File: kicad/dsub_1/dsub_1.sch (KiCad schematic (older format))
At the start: 3 parts, among them J1 DB15_Female, J2 DB15_Female, J3 DB25_Female

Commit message: geändert:       Doku/Anmerungen_fuer_Doku.odt 	geändert:       Doku/Tagebuch_Ziele.odt 	geändert:       abschlussprojekt/abschlussprojekt.ino -> Helligkeitssensor + LEDs implementiert 	geändert:       kicad/dsub_1/dsub_1.bak 	geändert:       kicad/dsub_1/dsub_1.pdf 	geändert:       kicad/dsub_1/dsub_1.sch
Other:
- note added: "Leistung:\nLüfter -> 12V/0,11A\nHeizung -> 12V/4,5A (55W)\nLEDs -> rot 12V/80mA; blau 12V/80mA\nPumpe -> 3-5V/100-200mA\n"
- note removed: "Leistung:\nLüfter -> 12V/0,11A\nHeizung -> 12V, 55W\nLEDs -> sehr wenig\nPumpe -> 3-5V/100-200mA\n"
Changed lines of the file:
@@
 Stecker:\nTorsten -> Männchen, Male\nFabian -> Weibchen, Female
 Text Notes 700  5250 0    79   ~ 0
-Leistung:\nLüfter  -> 12V/0,11A\nHeizung -> 12V, 55W\nLEDs   -> sehr wenig\nPumpe -> 3-5V/100-200mA\n
+Leistung:\nLüfter  -> 12V/0,11A\nHeizung -> 12V/4,5A  (55W)\nLEDs   -> rot 12V/80mA; blau 12V/80mA\nPumpe -> 3-5V/100-200mA\n
 $Comp
 L Connector:DB15_Female J2

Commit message: geändert:       abschlussprojekt/abschlussprojekt.ino 	gelöscht:       abschlussprojekt/update_limits.h 	neue Datei:     abschlussprojekt/update_messwerte.c 	neue Datei:     abschlussprojekt/update_messwerte.h 	geändert:       kicad/dsub_1/dsub_1-cache.lib 	geändert:       kicad/dsub_1/dsub_1.bak 	geändert:       kicad/dsub_1/dsub_1.pdf 	geändert:       kicad/dsub_1/dsub_1.sch
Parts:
- removed J1, J2: DB15_Female, symbol Connector:DB15_Female
- added J?: Conn_01x02, symbol Connector_Generic:Conn_01x02
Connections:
- net Heizung_minus: now also J?.1 (Pin_1); no longer J3.18 (P18)
- net Heizung_plus: now also J?.2 (Pin_2); no longer J3.19 (P19)
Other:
- note added: "Leistung:\nHeizung -> 12V/4,5A (55W)\nPumpe -> 3-5V/200-360mA\nLüfter -> 12V/0,11A\nLEDs -> rot 12V/80mA; blau 12V/80mA"
- note added: "extra Stecker, \nweil zuviel Strom für SubD"
- note removed: "Leistung:\nLüfter -> 12V/0,11A\nHeizung -> 12V/4,5A (55W)\nLEDs -> rot 12V/80mA; blau 12V/80mA\nPumpe -> 3-5V/100-200mA\n"
- note removed: "Signalkabel und stromführende Kabel\nin einem Stecker -> Problem Störungen, EMV ?"
- note removed: "Stecker Signale"
- note removed: "Stecker Stromführung"
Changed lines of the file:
@@
 Wire Wire Line
 	7950 3600 9550 3600
-$Comp
-L Connector:DB15_Female J1
-U 1 1 5D76075D
-P 5100 2500
-F 0 "J1" H 5007 1508 50  0000 C CNN
-F 1 "DB15_Female" H 5007 1599 50  0000 C CNN
-F 2 "" H 5100 2500 50  0001 C CNN
-F 3 " ~" H 5100 2500 50  0001 C CNN
-	1    5100 2500
-	1    0    0    1
-$EndComp
-Text GLabel 4500 3200 0    50   Input ~ 0
-Erdfeuchte1_plus
-Text GLabel 4500 3000 0    50   Input ~ 0
-Erdfeuchte1_minus
-Text GLabel 4500 2800 0    50   Input ~ 0
-Erdfeuchte2_plus
-Text GLabel 4500 2600 0    50   Input ~ 0
-Erdfeuchte2_minus
-Text GLabel 4500 2400 0    50   Input ~ 0
-Temperatursensor_plus
-Text GLabel 4500 2200 0    50   Input ~ 0
-Temperatursensor_minus
-Text GLabel 4500 2000 0    50   Input ~ 0
-Temperatursensor_data
-Text GLabel 4500 1800 0    50   Input ~ 0
-Fotowiderstand_plus
-Text GLabel 3500 3100 0    50   Input ~ 0
-Fotowiderstand_minus
-Text GLabel 3500 2900 0    50   Input ~ 0
-REED-Kontakt_plus
-Text GLabel 3500 2700 0    50   Input ~ 0
-REED-Kontakt_minus
-Text GLabel 3650 5550 0    50   Input ~ 0
-LED_plus
-Text GLabel 3650 5350 0    50   Input ~ 0
-LED_minus
-Text GLabel 4450 5650 0    50   Input ~ 0
-Pumpe1_plus
-Text GLabel 4450 5450 0    50   Input ~ 0
-Pumpe1_minus
-Text GLabel 4450 5250 0    50   Input ~ 0
-Pumpe2_plus
-Text GLabel 4450 5050 0    50   Input ~ 0
-Pumpe2_minus
-Text GLabel 4450 4850 0    50   Input ~ 0
-Lüfter_plus
-Text GLabel 4450 4650 0    50   Input ~ 0
-Lüfter_minus
-Wire Wire Line
-	4450 4850 4800 4850
-Wire Wire Line
-	4450 5050 4800 5050
-Wire Wire Line
-	4450 5250 4800 5250
-Wire Wire Line
-	4450 5450 4800 5450
-Wire Wire Line
-	4450 5650 4800 5650
-Wire Wire Line
-	4500 1800 4800 1800
-Wire Wire Line
-	4500 2000 4800 2000
-Wire Wire Line
-	4500 2200 4800 2200
-Wire Wire Line
-	4500 2400 4800 2400
-Wire Wire Line
-	4500 2600 4800 2600
-Wire Wire Line
-	4500 2800 4800 2800
-Wire Wire Line
-	3500 2700 4800 2700
-Wire Wire Line
-	4500 3000 4800 3000
-Wire Wire Line
-	4500 3200 4800 3200
-Wire Wire Line
-	3500 2900 4800 2900
-Wire Wire Line
-	3500 3100 4800 3100
-Text Notes 6750 1450 0    118  ~ 0
-Signalkabel und stromführende Kabel\nin einem Stecker -> Problem Störungen, EMV ?
-Wire Notes Line
-	6350 1150 6350 6300
-Text Notes 3650 1300 0    118  ~ 0
-Stecker Signale
-Text Notes 3650 3800 0    118  ~ 0
-Stecker Stromführung
-Text GLabel 7950 3400 0    50   Input ~ 0
+Text GLabel 2550 3550 0    50   Input ~ 0
 Heizung_plus
-Text GLabel 7950 3200 0    50   Input ~ 0
-Heizung_minus
-Wire Wire Line
-	7950 3400 9550 3400
-Wire Wire Line
-	7950 3200 9550 3200
-Text GLabel 4450 4450 0    50   Input ~ 0
-Heizung_plus
-Text GLabel 4450 4250 0    50   Input ~ 0
+Text GLabel 2550 3350 0    50   Input ~ 0
 Heizung_minus
 $Comp
@@
 Text Notes 1100 7100 0    157  Italic 0
 Stecker:\nTorsten -> Männchen, Male\nFabian -> Weibchen, Female
-Text Notes 700  5250 0    79   ~ 0
-Leistung:\nLüfter  -> 12V/0,11A\nHeizung -> 12V/4,5A  (55W)\nLEDs   -> rot 12V/80mA; blau 12V/80mA\nPumpe -> 3-5V/100-200mA\n
+Text Notes 7400 5750 0    79   ~ 0
+Leistung:\nHeizung -> 12V/4,5A  (55W)\nPumpe -> 3-5V/200-360mA\nLüfter  -> 12V/0,11A\nLEDs   -> rot 12V/80mA; blau 12V/80mA
+Text Notes 1950 3100 0    79   ~ 0
+extra Stecker, \nweil zuviel Strom für SubD
+Wire Notes Line
+	1700 2800 3800 2800
+Wire Notes Line
+	3800 2800 3800 3700
+Wire Notes Line
+	3800 3700 1700 3700
+Wire Notes Line
+	1700 3700 1700 2800
 $Comp
-L Connector:DB15_Female J2
-U 1 1 5D775ECC
-P 5100 4950
-F 0 "J2" H 5007 3958 50  0000 C CNN
-F 1 "DB15_Female" H 5007 4049 50  0000 C CNN
-F 2 "" H 5100 4950 50  0001 C CNN
-F 3 " ~" H 5100 4950 50  0001 C CNN
-	1    5100 4950
-	1    0    0    1
+L Connector_Generic:Conn_01x02 J?
+U 1 1 5D7EA451
+P 3200 3400
+F 0 "J?" H 3280 3392 50  0000 L CNN
+F 1 "Conn_01x02" H 3280 3301 50  0000 L CNN
+F 2 "" H 3200 3400 50  0001 C CNN
+F 3 "~" H 3200 3400 50  0001 C CNN
+	1    3200 3400
+	1    0    0    -1
 $EndComp
 Wire Wire Line
-	4450 4250 4800 4250
+	2550 3350 2800 3350
 Wire Wire Line
-	4450 4450 4800 4450
+	2800 3350 2800 3400
 Wire Wire Line
-	4450 4650 4800 4650
+	2800 3400 3000 3400
 Wire Wire Line
-	3650 5550 4800 5550
+	3000 3500 2800 3500
 Wire Wire Line
-	3650 5350 4800 5350
+	2800 3500 2800 3550
+Wire Wire Line
+	2800 3550 2550 3550
 $EndSCHEMATC

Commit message: geändert:       Doku/Anmerungen_fuer_Doku.odt 	neue Datei:     Doku/Anmerungen_fuer_Doku.pdf 	geändert:       Doku/Tagebuch_Ziele.odt 	geändert:       kicad/dsub_1/dsub_1.bak 	geändert:       kicad/dsub_1/dsub_1.pdf 	geändert:       kicad/dsub_1/dsub_1.sch 	geändert:       qelectrotech/verdrahtung/schematische_beschaltung.pdf 	geändert:       qelectrotech/verdrahtung/schematische_beschaltung.qet
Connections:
- net Fotowiderstand_data: now reaches J3.19 (P19)
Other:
- moved on the sheet: J3, J?
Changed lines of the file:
@@
 Sheet 1 1
 Title "Zuordnung Anschlüsse"
-Date "2019-08-14"
+Date "2019-09-26"
 Rev "0.2"
 Comp "STB AEA8"
@@
 Comment4 ""
 $EndDescr
-Text GLabel 9200 4700 0    50   Input ~ 0
+Text GLabel 3300 5450 0    50   Input ~ 0
 Erdfeuchte1_plus
 Wire Wire Line
-	9550 4700 9200 4700
-Text GLabel 9200 4500 0    50   Input ~ 0
+	3650 5450 3300 5450
+Text GLabel 3300 5250 0    50   Input ~ 0
 Erdfeuchte1_minus
 Wire Wire Line
-	9200 4500 9550 4500
-Text GLabel 9200 4300 0    50   Input ~ 0
+	3300 5250 3650 5250
+Text GLabel 3300 5050 0    50   Input ~ 0
 Erdfeuchte2_plus
-Text GLabel 9200 4100 0    50   Input ~ 0
+Text GLabel 3300 4850 0    50   Input ~ 0
 Erdfeuchte2_minus
-Text GLabel 9200 3900 0    50   Input ~ 0
+Text GLabel 3300 4650 0    50   Input ~ 0
 Temperatursensor_plus
-Text GLabel 9200 3700 0    50   Input ~ 0
+Text GLabel 3300 4450 0    50   Input ~ 0
 Temperatursensor_minus
-Text GLabel 9200 3500 0    50   Input ~ 0
+Text GLabel 3300 4250 0    50   Input ~ 0
 Temperatursensor_data
-Text GLabel 9200 3300 0    50   Input ~ 0
+Text GLabel 3300 4050 0    50   Input ~ 0
 Fotowiderstand_plus
-Text GLabel 9200 3100 0    50   Input ~ 0
+Text GLabel 3300 3850 0    50   Input ~ 0
 Fotowiderstand_minus
-Text GLabel 9200 2900 0    50   Input ~ 0
+Text GLabel 3300 3650 0    50   Input ~ 0
 REED-Kontakt_plus
-Text GLabel 9200 2700 0    50   Input ~ 0
+Text GLabel 3300 3450 0    50   Input ~ 0
 REED-Kontakt_minus
-Text GLabel 9200 2500 0    50   Input ~ 0
+Text GLabel 3300 3250 0    50   Input ~ 0
 LED_plus
-Text GLabel 9200 2300 0    50   Input ~ 0
+Text GLabel 3300 3050 0    50   Input ~ 0
 LED_minus
-Text GLabel 7950 4600 0    50   Input ~ 0
+Text GLabel 2050 5350 0    50   Input ~ 0
 Pumpe1_plus
-Text GLabel 7950 4400 0    50   Input ~ 0
+Text GLabel 2050 5150 0    50   Input ~ 0
 Pumpe1_minus
-Text GLabel 7950 4200 0    50   Input ~ 0
+Text GLabel 2050 4950 0    50   Input ~ 0
 Pumpe2_plus
-Text GLabel 7950 4000 0    50   Input ~ 0
+Text GLabel 2050 4750 0    50   Input ~ 0
 Pumpe2_minus
-Text GLabel 7950 3800 0    50   Input ~ 0
+Text GLabel 2050 4550 0    50   Input ~ 0
 Lüfter_plus
-Text GLabel 7950 3600 0    50   Input ~ 0
+Text GLabel 2050 4350 0    50   Input ~ 0
 Lüfter_minus
 Wire Wire Line
-	9550 2300 9200 2300
+	3650 3050 3300 3050
 Wire Wire Line
-	9550 2500 9200 2500
+	3650 3250 3300 3250
 Wire Wire Line
-	9550 2700 9200 2700
+	3650 3450 3300 3450
 Wire Wire Line
-	9200 2900 9550 2900
+	3300 3650 3650 3650
 Wire Wire Line
-	9200 3100 9550 3100
+	3300 3850 3650 3850
 Wire Wire Line
-	9200 3300 9550 3300
+	3300 4050 3650 4050
 Wire Wire Line
-	9200 3500 9550 3500
+	3300 4250 3650 4250
 Wire Wire Line
-	9200 3700 9550 3700
+	3300 4450 3650 4450
 Wire Wire Line
-	9200 3900 9550 3900
+	3300 4650 3650 4650
 Wire Wire Line
-	9200 4100 9550 4100
+	3300 4850 3650 4850
 Wire Wire Line
-	9200 4300 9550 4300
+	3300 5050 3650 5050
 Wire Wire Line
-	7950 4600 9550 4600
+	2050 5350 3650 5350
 Wire Wire Line
-	7950 4400 9550 4400
+	2050 5150 3650 5150
 Wire Wire Line
-	7950 4200 9550 4200
+	2050 4950 3650 4950
 Wire Wire Line
-	7950 4000 9550 4000
+	2050 4750 3650 4750
 Wire Wire Line
-	7950 3800 9550 3800
+	2050 4550 3650 4550
 Wire Wire Line
-	7950 3600 9550 3600
-Text GLabel 2550 3550 0    50   Input ~ 0
+	2050 4350 3650 4350
+Text GLabel 6800 4550 0    50   Input ~ 0
 Heizung_plus
-Text GLabel 2550 3350 0    50   Input ~ 0
+Text GLabel 6800 4350 0    50   Input ~ 0
 Heizung_minus
 $Comp
 L Connector:DB25_Female J3
 U 1 1 5D77214E
-P 9850 3500
-F 0 "J3" H 10029 3546 50  0000 L CNN
-F 1 "DB25_Female" H 10029 3455 50  0000 L CNN
-F 2 "" H 9850 3500 50  0001 C CNN
-F 3 " ~" H 9850 3500 50  0001 C CNN
-	1    9850 3500
+P 3950 4250
+F 0 "J3" H 4129 4296 50  0000 L CNN
+F 1 "DB25_Female" H 4129 4205 50  0000 L CNN
+F 2 "" H 3950 4250 50  0001 C CNN
+F 3 " ~" H 3950 4250 50  0001 C CNN
+	1    3950 4250
 	1    0    0    -1
 $EndComp
-Text Notes 1100 7100 0    157  Italic 0
+Text Notes 900  7350 0    157  Italic 0
 Stecker:\nTorsten -> Männchen, Male\nFabian -> Weibchen, Female
-Text Notes 7400 5750 0    79   ~ 0
+Text Notes 950  1400 0    79   ~ 0
 Leistung:\nHeizung -> 12V/4,5A  (55W)\nPumpe -> 3-5V/200-360mA\nLüfter  -> 12V/0,11A\nLEDs   -> rot 12V/80mA; blau 12V/80mA
-Text Notes 1950 3100 0    79   ~ 0
+Text Notes 6200 4100 0    79   ~ 0
 extra Stecker, \nweil zuviel Strom für SubD
 Wire Notes Line
-	1700 2800 3800 2800
+	5950 3800 8050 3800
 Wire Notes Line
-	3800 2800 3800 3700
+	8050 3800 8050 4700
 Wire Notes Line
-	3800 3700 1700 3700
+	8050 4700 5950 4700
 Wire Notes Line
-	1700 3700 1700 2800
+	5950 4700 5950 3800
 $Comp
 L Connector_Generic:Conn_01x02 J?
 U 1 1 5D7EA451
-P 3200 3400
-F 0 "J?" H 3280 3392 50  0000 L CNN
-F 1 "Conn_01x02" H 3280 3301 50  0000 L CNN
-F 2 "" H 3200 3400 50  0001 C CNN
-F 3 "~" H 3200 3400 50  0001 C CNN
-	1    3200 3400
+P 7450 4400
+F 0 "J?" H 7530 4392 50  0000 L CNN
+F 1 "Conn_01x02" H 7530 4301 50  0000 L CNN
+F 2 "" H 7450 4400 50  0001 C CNN
+F 3 "~" H 7450 4400 50  0001 C CNN
+	1    7450 4400
 	1    0    0    -1
 $EndComp
 Wire Wire Line
-	2550 3350 2800 3350
+	6800 4350 7050 4350
 Wire Wire Line
-	2800 3350 2800 3400
+	7050 4350 7050 4400
 Wire Wire Line
-	2800 3400 3000 3400
+	7050 4400 7250 4400
 Wire Wire Line
-	3000 3500 2800 3500
+	7250 4500 7050 4500
 Wire Wire Line
-	2800 3500 2800 3550
+	7050 4500 7050 4550
 Wire Wire Line
-	2800 3550 2550 3550
+	7050 4550 6800 4550
+Text GLabel 2050 4150 0    50   Input ~ 0
+Fotowiderstand_data
+Wire Wire Line
+	2050 4150 3650 4150
 $EndSCHEMATC

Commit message: geändert:       Doku/Tagebuch_Ziele.odt 	neue Datei:     Doku/Tagebuch_Ziele.pdf 	geändert:       abschlussprojekt/abschlussprojekt.ino 	gelöscht:       abschlussprojekt/update_messwerte.cpp 	gelöscht:       abschlussprojekt/update_messwerte.h 	geändert:       kicad/dsub_1/dsub_1.bak 	geändert:       kicad/dsub_1/dsub_1.pdf 	geändert:       kicad/dsub_1/dsub_1.sch 	geändert:       lib_fabi/update_messwerte.cpp 	geändert:       lib_fabi/update_messwerte.h
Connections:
- net Fotowiderstand_data: no longer names the net of J3.19 (P19)
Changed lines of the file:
@@
 Wire Wire Line
 	7050 4550 6800 4550
-Text GLabel 2050 4150 0    50   Input ~ 0
-Fotowiderstand_data
-Wire Wire Line
-	2050 4150 3650 4150
 $EndSCHEMATC

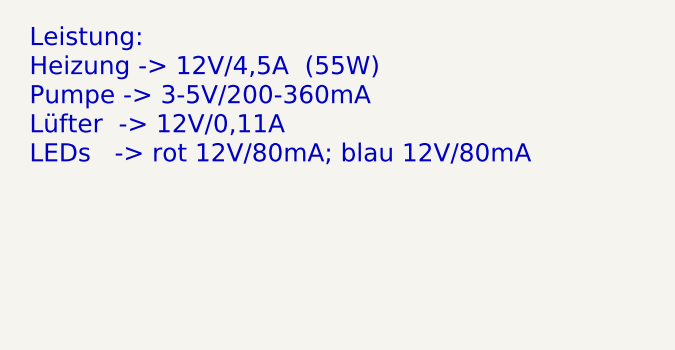
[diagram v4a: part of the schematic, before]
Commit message: geändert:       kicad/dsub_1/dsub_1.pdf 	geändert:       kicad/dsub_1/dsub_1.sch 	geändert:       kicad/dsub_1/dsub_1.sch-bak
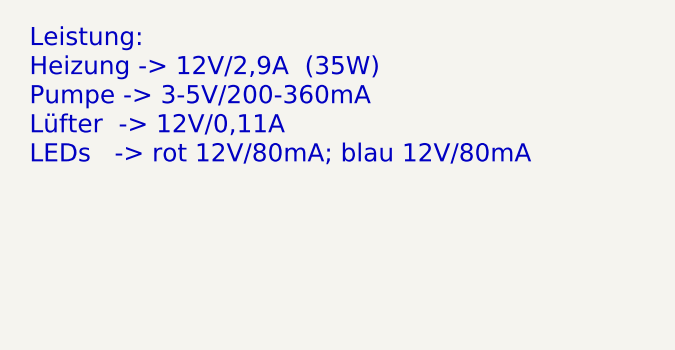
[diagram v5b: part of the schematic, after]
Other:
- note added: "Leistung:\nHeizung -> 12V/2,9A (35W)\nPumpe -> 3-5V/200-360mA\nLüfter -> 12V/0,11A\nLEDs -> rot 12V/80mA; blau 12V/80mA"
- note removed: "Leistung:\nHeizung -> 12V/4,5A (55W)\nPumpe -> 3-5V/200-360mA\nLüfter -> 12V/0,11A\nLEDs -> rot 12V/80mA; blau 12V/80mA"
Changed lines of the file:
@@
 EESchema Schematic File Version 4
 LIBS:dsub_1-cache
-EELAYER 26 0
+EELAYER 30 0
 EELAYER END
 $Descr A4 11693 8268
@@
 Sheet 1 1
 Title "Zuordnung Anschlüsse"
-Date "2019-09-26"
+Date "2019-11-20"
 Rev "0.2"
 Comp "STB AEA8"
@@
 Stecker:\nTorsten -> Männchen, Male\nFabian -> Weibchen, Female
 Text Notes 950  1400 0    79   ~ 0
-Leistung:\nHeizung -> 12V/4,5A  (55W)\nPumpe -> 3-5V/200-360mA\nLüfter  -> 12V/0,11A\nLEDs   -> rot 12V/80mA; blau 12V/80mA
+Leistung:\nHeizung -> 12V/2,9A  (35W)\nPumpe -> 3-5V/200-360mA\nLüfter  -> 12V/0,11A\nLEDs   -> rot 12V/80mA; blau 12V/80mA
 Text Notes 6200 4100 0    79   ~ 0
 extra Stecker, \nweil zuviel Strom für SubD
